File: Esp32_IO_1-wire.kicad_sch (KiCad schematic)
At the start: 29 parts, among them J1 IO-pins, J2 1-Wire, J3 Vin, J4 I2C, J5 GPIO -pins, J6 RX/TX, U1 DS2484R, U2 PCF8574AT, U3 ESP32_S3_supermini

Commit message: Signed-off-by: regamp <patbence1999@gmail.com>
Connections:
- no-connect marks 0 -> 4
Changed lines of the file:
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@@
 		(color 0 0 0 0)
 	)
+	(no_connect
+		(at 45.72 166.37)
+	)
+	(no_connect
+		(at 49.53 38.1)
+	)
+	(no_connect
+		(at 45.72 163.83)
+	)
+	(no_connect
+		(at 45.72 168.91)
+	)
 	(wire
 		(pts
@@
 	(wire
 		(pts
+			(xy 46.99 143.51) (xy 45.72 143.51)
+		)
+		(stroke
+			(width 0)
+			(type default)
+		)
+	)
+	(wire
+		(pts
 			(xy 209.55 38.1) (xy 195.58 38.1)
 		)
@@
 	(wire
 		(pts
+			(xy 46.99 161.29) (xy 45.72 161.29)
+		)
+		(stroke
+			(width 0)
+			(type default)
+		)
+	)
+	(wire
+		(pts
 			(xy 31.75 41.91) (xy 31.75 55.88)
 		)
@@
 	(wire
 		(pts
+			(xy 46.99 146.05) (xy 45.72 146.05)
+		)
+		(stroke
+			(width 0)
+			(type default)
+		)
+	)
+	(wire
+		(pts
 			(xy 54.61 139.7) (xy 59.69 139.7)
 		)
@@
 	(wire
 		(pts
+			(xy 46.99 138.43) (xy 45.72 138.43)
+		)
+		(stroke
+			(width 0)
+			(type default)
+		)
+	)
+	(wire
+		(pts
 			(xy 195.58 54.61) (xy 195.58 64.77)
 		)
@@
 	(wire
 		(pts
+			(xy 46.99 148.59) (xy 45.72 148.59)
+		)
+		(stroke
+			(width 0)
+			(type default)
+		)
+	)
+	(wire
+		(pts
 			(xy 195.58 46.99) (xy 195.58 38.1)
 		)
@@
 	(wire
 		(pts
+			(xy 46.99 158.75) (xy 45.72 158.75)
+		)
+		(stroke
+			(width 0)
+			(type default)
+		)
+	)
+	(wire
+		(pts
 			(xy 20.32 154.94) (xy 20.32 149.86)
 		)
@@
 	(wire
 		(pts
+			(xy 45.72 140.97) (xy 46.99 140.97)
+		)
+		(stroke
+			(width 0)
+			(type default)
+		)
+	)
+	(wire
+		(pts
 			(xy 21.59 25.4) (xy 31.75 25.4)
 		)
@@
 		(pts
 			(xy 149.86 49.53) (xy 161.29 49.53)
+		)
+		(stroke
+			(width 0)
+			(type default)
+		)
+	)
+	(wire
+		(pts
+			(xy 46.99 156.21) (xy 45.72 156.21)
 		)
 		(stroke
@@
 	)
 	(label "GPIO4"
-		(at 45.72 146.05 0)
+		(at 46.99 146.05 0)
 		(effects
 			(font
@@
 	)
 	(label "GPIO3"
-		(at 45.72 143.51 0)
+		(at 46.99 143.51 0)
 		(effects
 			(font
@@
 	)
 	(label "GPIO10"
-		(at 45.72 161.29 0)
+		(at 46.99 161.29 0)
 		(effects
 			(font
@@
 	)
 	(label "GPIO9"
-		(at 45.72 158.75 0)
+		(at 46.99 158.75 0)
 		(effects
 			(font
@@
 	)
 	(label "GPIO5"
-		(at 45.72 148.59 0)
+		(at 46.99 148.59 0)
 		(effects
 			(font
@@
 	)
 	(label "GPIO8"
-		(at 45.72 156.21 0)
+		(at 46.99 156.21 0)
 		(effects
 			(font
@@
 	)
 	(label "GPIO1"
-		(at 45.72 138.43 0)
+		(at 46.99 138.43 0)
 		(effects
 			(font
@@
 	)
 	(label "GPIO2"
-		(at 45.72 140.97 0)
-		(effects
-			(font
+		(at 46.99 140.97 0)
+		(effects
+			(font

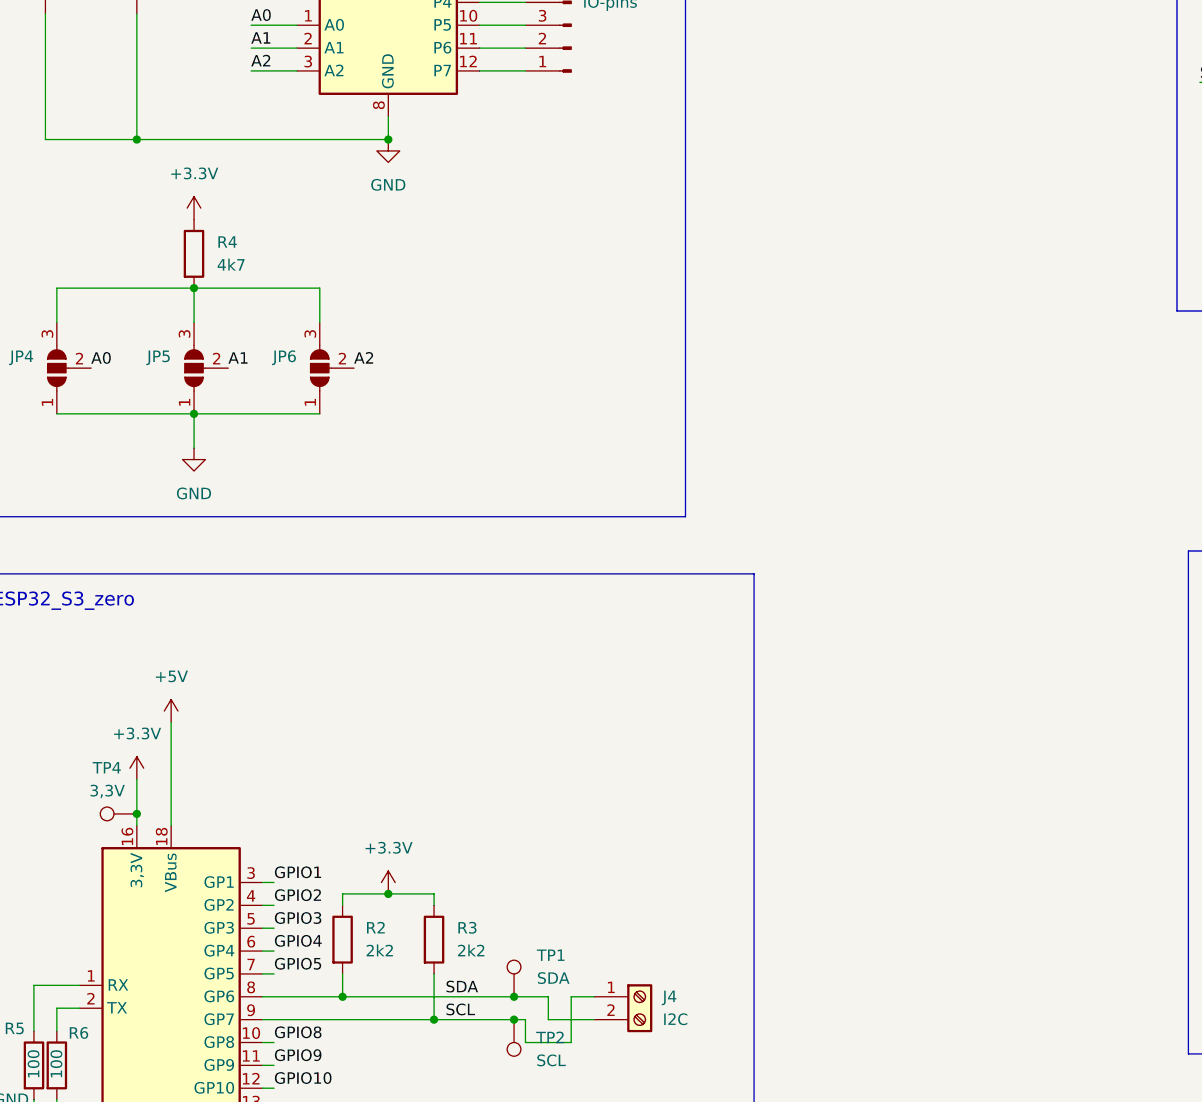
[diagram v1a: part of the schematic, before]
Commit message: I2C Bus with 1,27mm pinheader
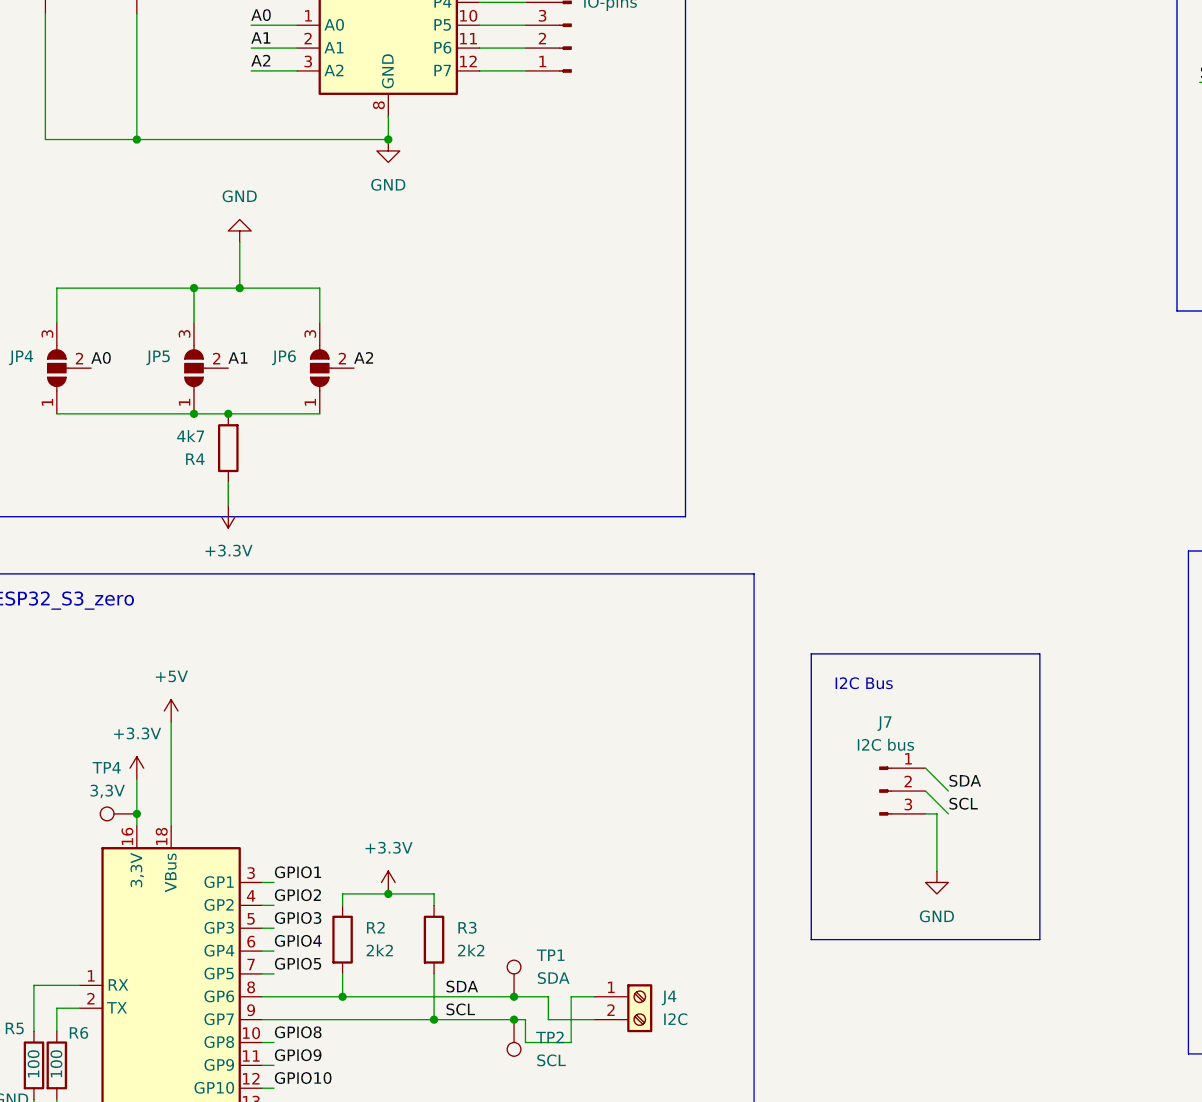
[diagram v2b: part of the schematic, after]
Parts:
- added J7: I2C bus, Connector_PinHeader_1.27mm:PinHeader_1x03_P1.27mm_Horizontal, symbol Connector:Conn_01x03_Pin
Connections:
- net GND: now also JP4.3 (B), JP5.3 (B), JP6.3 (B), J7.3 (Pin_3); no longer JP4.1 (A), JP5.1 (A), JP6.1 (A)
- new net: JP4.1 (A), JP5.1 (A), JP6.1 (A), R4.2
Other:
- note added: "I2C Bus"
- moved on the sheet: R4
